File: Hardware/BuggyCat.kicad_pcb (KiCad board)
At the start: 2 copper layers, 36.8 x 104 mm, 104 parts, among them J1 Antenna, J2 BG306-02-A-2-0400-L-G, J3 Header7, J4 Header 2, J5 Header 4, J6 Input Power:2x AA Battery, P1 USB_C_Plug_USB2.0, Q1 AO3422, Q2 AO3422, Q3 LDA111STR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

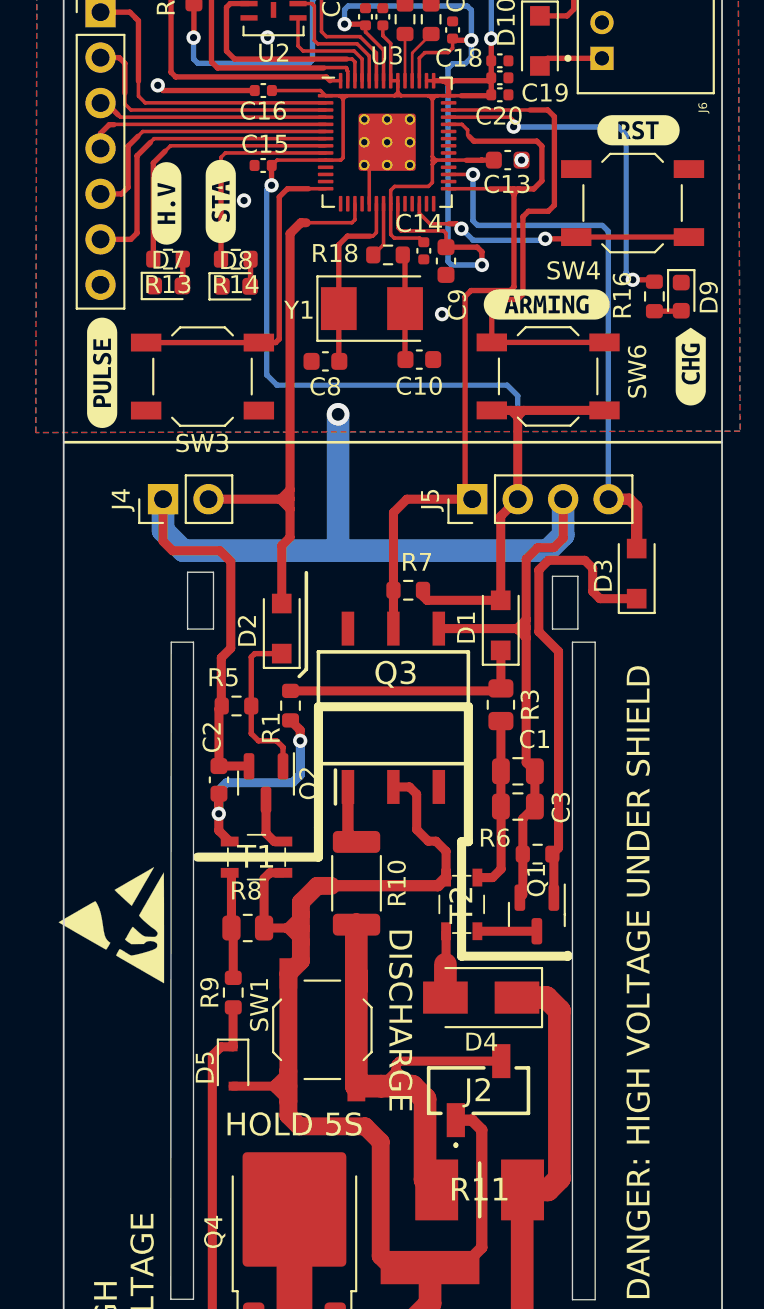
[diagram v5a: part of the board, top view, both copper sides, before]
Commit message: SW1, SW3 and SW6 buttons changed
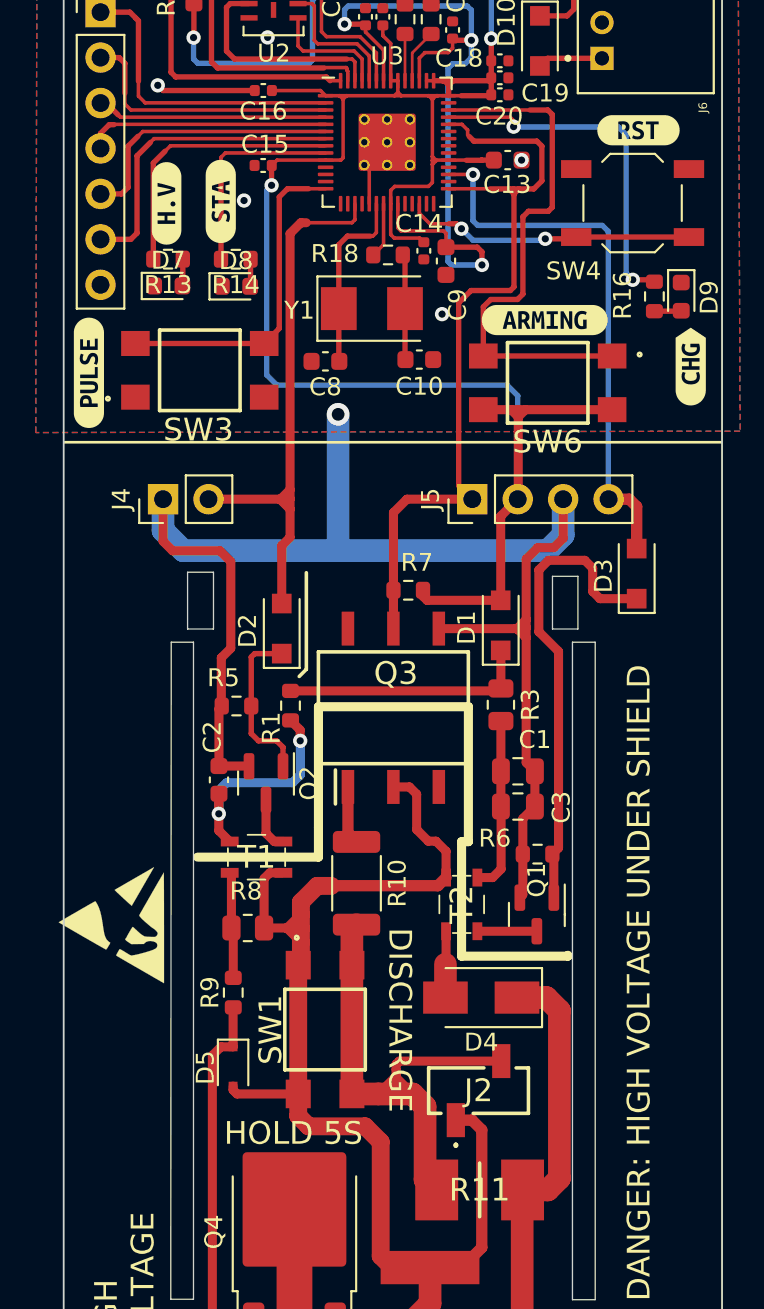
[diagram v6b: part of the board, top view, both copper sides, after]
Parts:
- SW1, SW3, SW6: footprint Button_Switch_SMD:SW_SPST_TL3342 -> BuggyCat:TL3305AF160QG
- moved kibuzzard-642E11AF 0.88 mm to (74.8, 56.0)
- moved kibuzzard-642F0B74 0.74 mm to (49.3, 58.9)
- moved SW3 0.38 mm to (55.5, 58.8), turned to 0 degrees
- moved SW6 0.36 mm to (74.9, 59.5), turned to 180 degrees
- moved SW1 0.15 mm to (62.5, 95.7), turned to -90 degrees
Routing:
- net Net-(D5-A): track 76.2 -> 74.2 mm
- net /GP28: track 27.7 -> 29.7 mm
- net +3V3: track 152.5 -> 153.7 mm
- net Net-(J2-Pin_2): track 29.1 -> 29.7 mm

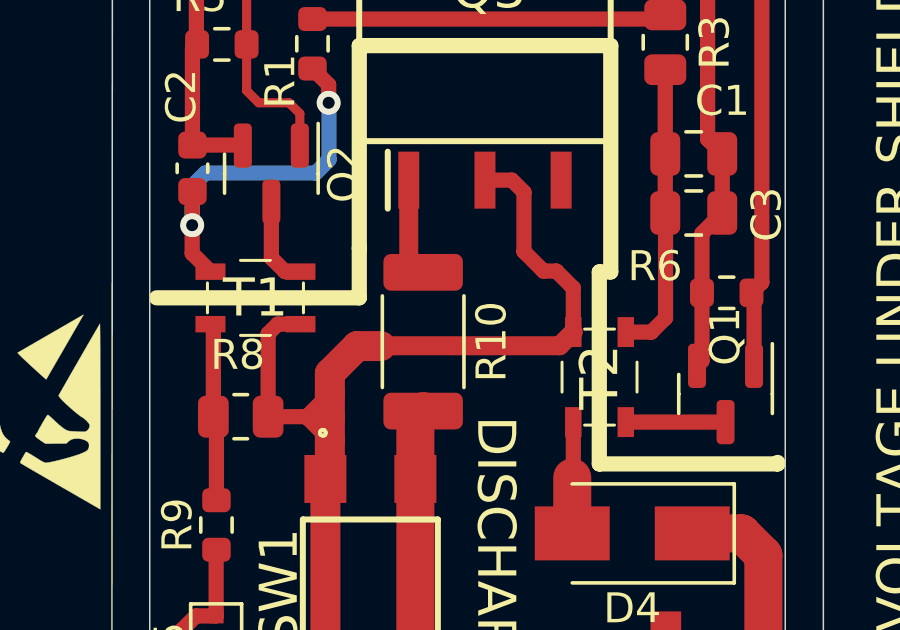
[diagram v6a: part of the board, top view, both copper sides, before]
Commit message: Footprint of T1 and T2 edited
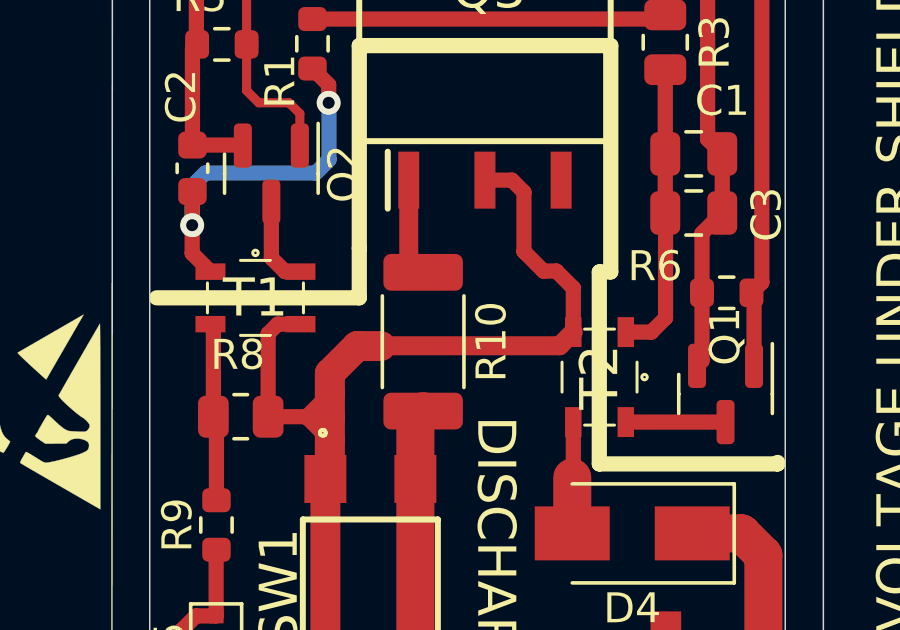
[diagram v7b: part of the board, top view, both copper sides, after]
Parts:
- SW1, SW3, SW6: value TL3342F450QG -> TL3305AF260QG
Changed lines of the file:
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@@
     (descr "TO-252/DPAK SMD package, http://www.infineon.com/cms/en/product/packages/PG-TO252/PG-TO252-3-1/")
     (tags "DPAK TO-252 DPAK-3 TO-252-3 SOT-428")
-    (property "Manf#" "RGT16NL65DGTL")
+    (property "Manf#" "RGT16BM65DTL")
     (property "Proveedor" "MOUSER")
     (property "Sheetfile" "BuggyCat.kicad_sch")
@@
     (descr "TL3305AF160QG")
     (tags "Switch")
-    (property "LCSC#" "C2886897")
-    (property "Manf#" "TL3342F450QG")
+    (property "LCSC#" "")
+    (property "Manf#" "TL3305AF260QG")
     (property "Proveedor" "MOUSER")
     (property "Sheetfile" "BuggyCat.kicad_sch")
@@
         (effects (font (size 1.27 1.27) (thickness 0.254)))
     )
-    (fp_text value "TL3342F450QG" (at -0.358 0.874) (layer "F.SilkS") hide
+    (fp_text value "TL3305AF260QG" (at -0.358 0.874) (layer "F.SilkS") hide
         (effects (font (size 1.27 1.27) (thickness 0.254)))
     )
@@
     (descr "SMD Crystal SERIES SMD2520/2 http://www.icbase.com/File/PDF/HKC/HKC00061008.pdf, 5.0x3.2mm^2 package")
     (tags "SMD SMT crystal")
-    (property "LCSC#" "C709001")
-    (property "Proveedor" "LCSC")
+    (property "LCSC#" "")
+    (property "Manf#" "445I23D12M00000")
+    (property "Proveedor" "MOUSER")
     (property "Sheetfile" "BuggyCat.kicad_sch")
     (property "Sheetname" "")
@@
     (fp_line (start 1.6 0.5) (end 1.6 -0.5)
       (stroke (width 0.1) (type solid)) (layer "F.SilkS"))
+    (fp_circle (center 0 1.5) (end 0.075 1.55)
+      (stroke (width 0.1) (type default)) (fill none) (layer "F.SilkS"))
     (fp_line (start -2.8 -2.05) (end 2.8 -2.05)
       (stroke (width 0.1) (type solid)) (layer "F.CrtYd"))
@@
     (pad "4" smd rect (at 1.5 0.875 270) (size 0.55 1) (layers "F.Cu" "F.Paste" "F.Mask")
       (net 78 "Net-(T1-AA)") (pinfunction "AA") (pintype "passive"))
-    (model "${KIPRJMOD}/Library/3D/ATB322524-0110-T000.step"
+    (model "ATB322524-0110-T000.stp"
       (offset (xyz 0 0 0))
       (scale (xyz 1 1 1))
@@
     (descr "TL3305AF160QG")
     (tags "Switch")
-    (property "LCSC#" "C2886897")
-    (property "Manf#" "TL3342F450QG")
+    (property "LCSC#" "")
+    (property "Manf#" "TL3305AF260QG")
     (property "Proveedor" "MOUSER")
     (property "Sheetfile" "BuggyCat.kicad_sch")
@@
         (effects (font (size 1.27 1.27) (thickness 0.254)))
     )
-    (fp_text value "TL3342F450QG" (at -0.358 0.874) (layer "F.SilkS") hide
+    (fp_text value "TL3305AF260QG" (at -0.358 0.874) (layer "F.SilkS") hide
         (effects (font (size 1.27 1.27) (thickness 0.254)))
     )
@@
     (descr "TL3305AF160QG")
     (tags "Switch")
-    (property "LCSC#" "C2886897")
-    (property "Manf#" "TL3342F450QG")
+    (property "LCSC#" "")
+    (property "Manf#" "TL3305AF260QG")
     (property "Proveedor" "MOUSER")
     (property "Sheetfile" "BuggyCat.kicad_sch")
@@
         (effects (font (size 1.27 1.27) (thickness 0.254)))
     )
-    (fp_text value "TL3342F450QG" (at -0.358 0.874 90) (layer "F.SilkS") hide
+    (fp_text value "TL3305AF260QG" (at -0.358 0.874 90) (layer "F.SilkS") hide
         (effects (font (size 1.27 1.27) (thickness 0.254)))
     )
@@
     (fp_line (start 1.6 0.5) (end 1.6 -0.5)
       (stroke (width 0.1) (type solid)) (layer "F.SilkS"))
+    (fp_circle (center 0 1.5) (end 0.075 1.55)
+      (stroke (width 0.1) (type default)) (fill none) (layer "F.SilkS"))
     (fp_line (start -2.8 -2.05) (end 2.8 -2.05)
       (stroke (width 0.1) (type solid)) (layer "F.CrtYd"))
@@
     (pad "4" smd rect (at 1.5 0.875 180) (size 0.55 1) (layers "F.Cu" "F.Paste" "F.Mask")
       (net 1 "Net-(T2-AA)") (pinfunction "AA") (pintype "passive"))
-    (model "${KIPRJMOD}/Library/3D/ATB322524-0110-T000.step"
+    (model "ATB322524-0110-T000.stp"
       (offset (xyz 0 0 0))
       (scale (xyz 1 1 1))

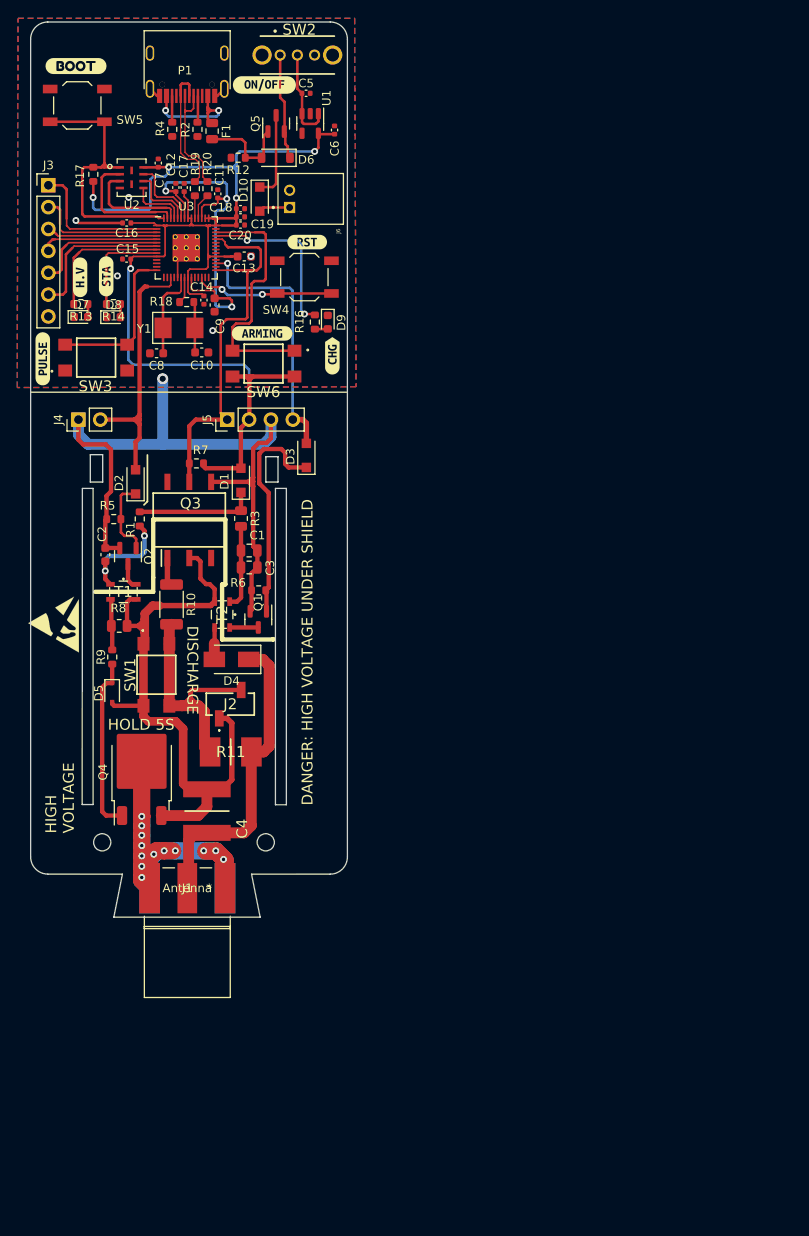
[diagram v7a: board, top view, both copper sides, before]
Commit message: New board proposal with 3 battery holder
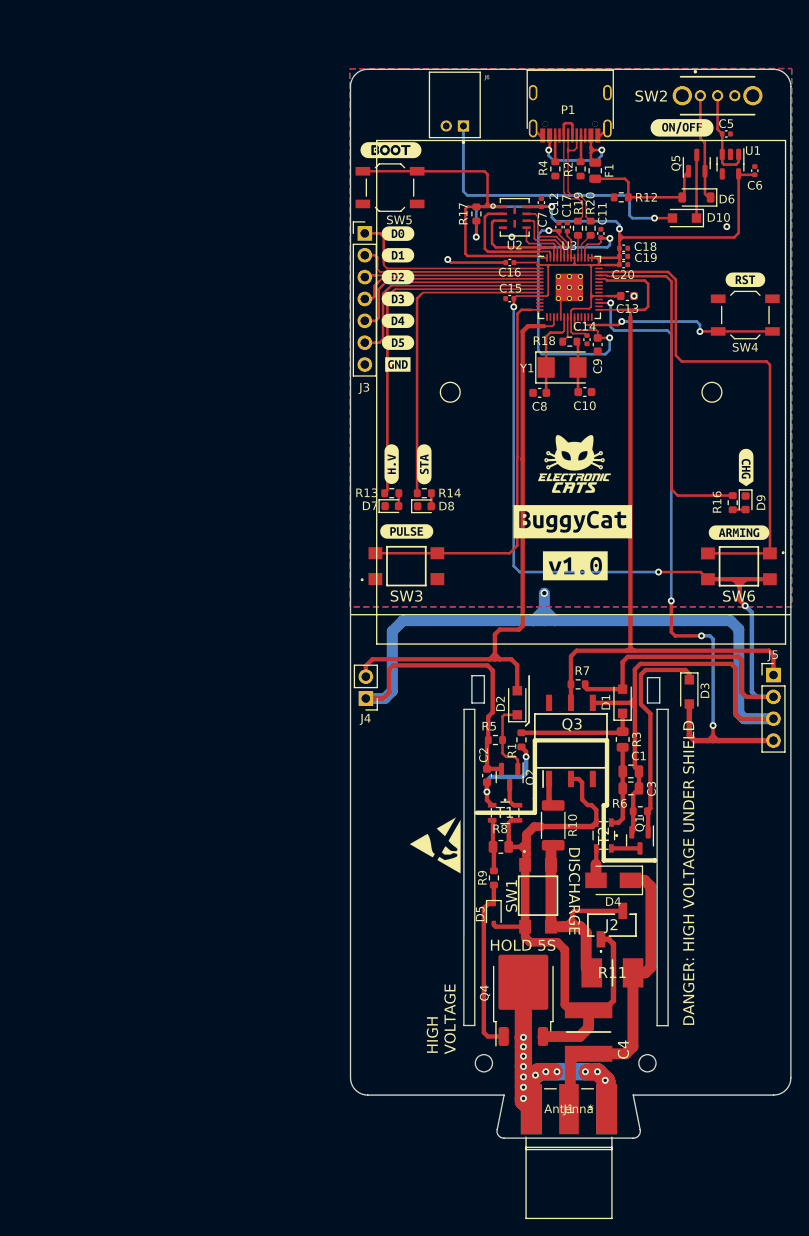
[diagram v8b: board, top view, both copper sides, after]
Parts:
- added REF**: BatteryHolder, BuggyCat:BatteryHolder, F.Cu at (111.8, 62.8)
- G***, kibuzzard-642DF7A2, kibuzzard-642DF7B5, kibuzzard-642DF7CA, kibuzzard-642DF7D8, kibuzzard-642DF7E6, kibuzzard-642DF805, kibuzzard-642DF817, kibuzzard-642E0E1B, kibuzzard-642E0E2F: moved to F.Cu
- moved REF** 74.0 mm to (131.1, 125.3)
- moved J5 70.1 mm to (134.2, 95.7), turned to 0 degrees
- moved kibuzzard-642E0B91 68.0 mm to (128.6, 95.7), turned to 180 degrees
- moved kibuzzard-642E0B82 67.7 mm to (130.2, 98.2), turned to 180 degrees
- moved kibuzzard-642E0B26 66.9 mm to (130.2, 100.7), turned to 180 degrees
- moved kibuzzard-642E0AF5 66.4 mm to (129.4, 103.3), turned to 180 degrees
- moved kibuzzard-642E11AF 60.1 mm to (130.2, 79.1)
- moved SW6 60.0 mm to (130.2, 83.0)
- moved kibuzzard-642E0E2F 56.0 mm to (111.2, 83.0), turned to 0 degrees
- moved kibuzzard-642E0E1B 55.0 mm to (110.9, 77.9), turned to 0 degrees
- moved G*** 55.0 mm to (111.1, 71.2), turned to 0 degrees
- moved D9 52.9 mm to (131.0, 75.7)
- moved R16 52.9 mm to (129.5, 75.7)
- moved kibuzzard-642E0AD5 52.7 mm to (91.1, 98.4), turned to 180 degrees
- moved D3 52.3 mm to (124.4, 97.6), turned to -90 degrees
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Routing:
- net GND: track 96.0 -> 164.1 mm, vias 6 -> 5
- net +3V3: track 153.7 -> 212.4 mm, vias 5 -> 6
- net /HVPWM: track 30.8 -> 78.7 mm, vias 1 -> 4
- net /CHARGED: track 45.4 -> 88.5 mm
- net /HVPULSE: track 31.9 -> 69.7 mm
- net Net-(D10-A): track 3.64 -> 34.3 mm, vias 0 -> 1
- net /GP28: track 29.7 -> 58.6 mm
- net /GP11: track 18.5 -> 46.6 mm
- net /GP6: track 15.4 -> 41.1 mm
- net /GP7: track 11.6 -> 37.2 mm
- net /GP27: track 20.0 -> 40.3 mm, vias 2 -> 0
- net /GP4: track 15.4 -> 24.1 mm
- net +1V2: track 42.3 -> 51.1 mm
- net /GP5: track 17.5 -> 26.2 mm
- net /GP3: track 13.6 -> 22.0 mm
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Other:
- board size 36.8 x 104 mm -> 51.2 x 124.2 mm
